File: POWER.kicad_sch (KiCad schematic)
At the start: 26 parts, among them J14 USB_C_Receptacle_USB2.0_16P, U10 REF3033, U11 RY8411, U12 XC6210B332MR, U9 USBLC6-2SC6

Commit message: finish
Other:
- moved on the sheet: C66, R51, U10

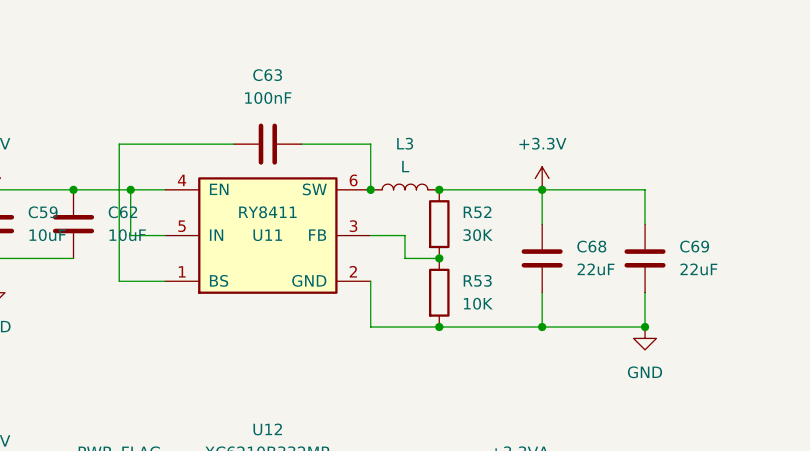
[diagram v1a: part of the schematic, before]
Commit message: 修改错误引脚
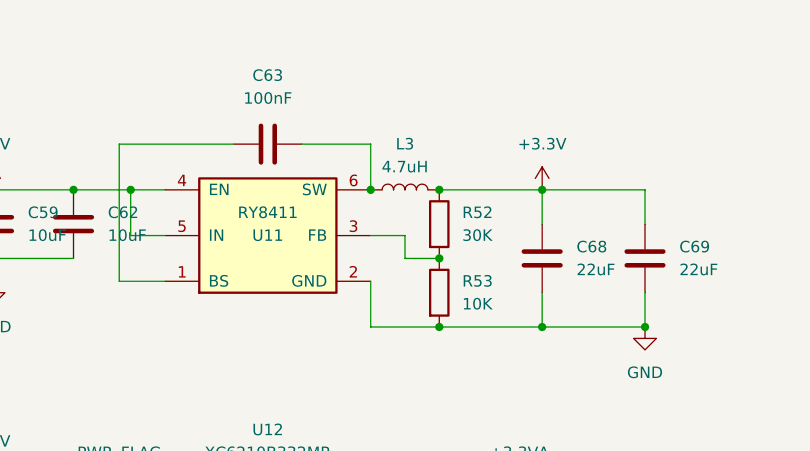
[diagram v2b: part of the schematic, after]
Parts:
- L3: value L -> 4.7uH
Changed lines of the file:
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@@
 			)
 		)
-		(property "Value" "L"
+		(property "Value" "4.7uH"
 			(at 203.2 53.34 90)
 			(show_name no)
